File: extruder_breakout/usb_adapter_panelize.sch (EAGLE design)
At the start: 6 parts, among them X1 9090-4V, X2 PN87520-S, X3 22-23-2031, X4 22-23-2031

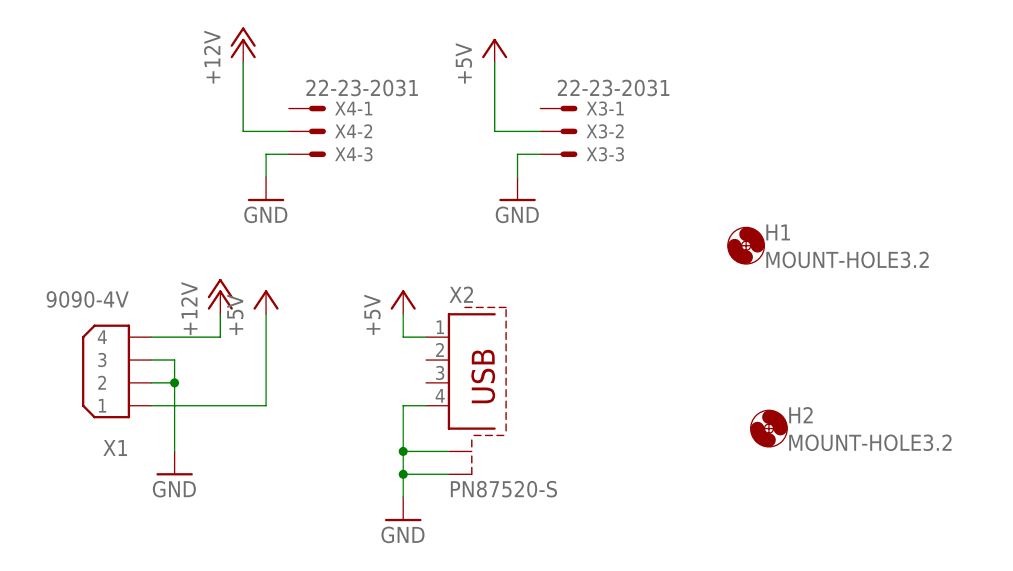
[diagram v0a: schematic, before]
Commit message: behebt kleine Fehler im Stromverteiler-Board
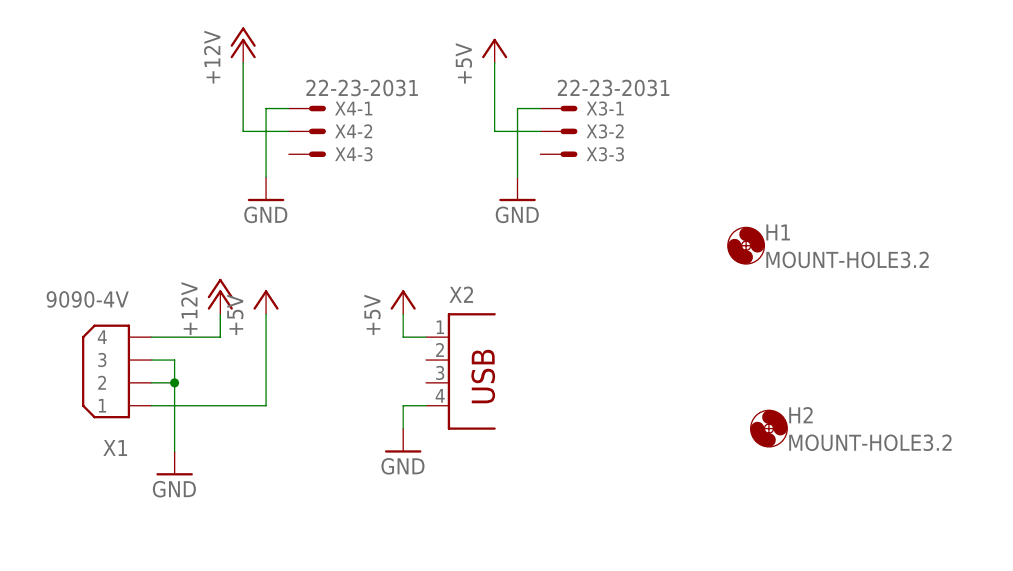
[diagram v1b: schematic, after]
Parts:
- X2: value PN87520-S -> (none); device con-berg:PN87520-S -> con-berg:PN87520
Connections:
- net GND: now also X3-1.S, X4-1.S; no longer X2.S1, X2.S2, X3-3.S, X4-3.S
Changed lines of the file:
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@@
 <parts>
 <part name="X1" library="con-thomas-betts" deviceset="9090-4" device="V"/>
-<part name="X2" library="con-berg" deviceset="PN87520-S" device=""/>
+<part name="X2" library="con-berg" deviceset="PN87520" device=""/>
 <part name="X3" library="con-molex" deviceset="22-23-2031" device=""/>
 <part name="X4" library="con-molex" deviceset="22-23-2031" device=""/>
@@
 <instance part="H2" gate="G$1" x="91.44" y="17.78"/>
 <instance part="GND1" gate="1" x="25.4" y="12.7"/>
-<instance part="GND2" gate="1" x="50.8" y="7.62"/>
+<instance part="GND2" gate="1" x="50.8" y="15.24"/>
 <instance part="GND3" gate="1" x="63.5" y="43.18"/>
 <instance part="GND4" gate="1" x="35.56" y="43.18"/>
@@
 <nets>
 <net name="GND" class="0">
+<segment>
+<pinref part="GND4" gate="1" pin="GND"/>
+<wire x1="35.56" y1="45.72" x2="35.56" y2="53.34" width="0.1524" layer="91"/>
+<pinref part="X4" gate="-1" pin="S"/>
+<wire x1="35.56" y1="53.34" x2="38.1" y2="53.34" width="0.1524" layer="91"/>
+</segment>
+<segment>
+<pinref part="GND3" gate="1" pin="GND"/>
+<wire x1="63.5" y1="45.72" x2="63.5" y2="53.34" width="0.1524" layer="91"/>
+<pinref part="X3" gate="-1" pin="S"/>
+<wire x1="63.5" y1="53.34" x2="66.04" y2="53.34" width="0.1524" layer="91"/>
+</segment>
 <segment>
 <pinref part="X1" gate="G$1" pin="3"/>
@@
 <pinref part="GND2" gate="1" pin="GND"/>
 <wire x1="53.34" y1="20.32" x2="50.8" y2="20.32" width="0.1524" layer="91"/>
-<wire x1="50.8" y1="20.32" x2="50.8" y2="15.24" width="0.1524" layer="91"/>
-<pinref part="X2" gate="G$1" pin="S2"/>
-<wire x1="50.8" y1="15.24" x2="50.8" y2="12.7" width="0.1524" layer="91"/>
-<wire x1="50.8" y1="12.7" x2="50.8" y2="10.16" width="0.1524" layer="91"/>
-<wire x1="55.88" y1="12.7" x2="50.8" y2="12.7" width="0.1524" layer="91"/>
-<junction x="50.8" y="12.7"/>
-<pinref part="X2" gate="G$1" pin="S1"/>
-<wire x1="55.88" y1="15.24" x2="50.8" y2="15.24" width="0.1524" layer="91"/>
-<junction x="50.8" y="15.24"/>
-</segment>
-<segment>
-<pinref part="X4" gate="-3" pin="S"/>
-<wire x1="38.1" y1="48.26" x2="35.56" y2="48.26" width="0.1524" layer="91"/>
-<pinref part="GND4" gate="1" pin="GND"/>
-<wire x1="35.56" y1="48.26" x2="35.56" y2="45.72" width="0.1524" layer="91"/>
-</segment>
-<segment>
-<pinref part="X3" gate="-3" pin="S"/>
-<wire x1="66.04" y1="48.26" x2="63.5" y2="48.26" width="0.1524" layer="91"/>
-<pinref part="GND3" gate="1" pin="GND"/>
-<wire x1="63.5" y1="48.26" x2="63.5" y2="45.72" width="0.1524" layer="91"/>
+<wire x1="50.8" y1="20.32" x2="50.8" y2="17.78" width="0.1524" layer="91"/>
 </segment>
 </net>
